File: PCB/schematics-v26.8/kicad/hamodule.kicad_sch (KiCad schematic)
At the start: 192 parts, among them J1 GND|5V, J10 Tx|Rx, J11 Sda|Scl, J12 3|9, J13 13|12, J14 3.3v|GND|7|15, J15 2604-1104, J16 2604-1104, J17 TestPoint, J19 TestPoint, J2 2604-1102, J3 USB_C_Receptacle_USB2.0, J4 GND|3.3V, J5 Conn_01x02_Pin, J6 2604-1104, J7 2604-1104, J8 5v|GND|Do, J9 Screen, K1 AQG22205, K2 AQG22205, K3 AQG22205, K4 AQG22205, K5 AQG22205, K6 AQG22205, K7 AQG22205, K8 AQG22205, SW1 USB | PS, SW2 Reset, SW3 Boot, U1 LD1117AV33, U10 SN74LV1T34DBV, U11 ULN2803A, U12 TCAL6416, U14 74AHC1G04, U2 USBLC6-2SC6, U3 ESP32-S3-WROOM-2, U4 LDA210, U5 LDA210, U6 LDA210, U7 LDA210, U8 SHT4x, U9 SN74LVCH8T245

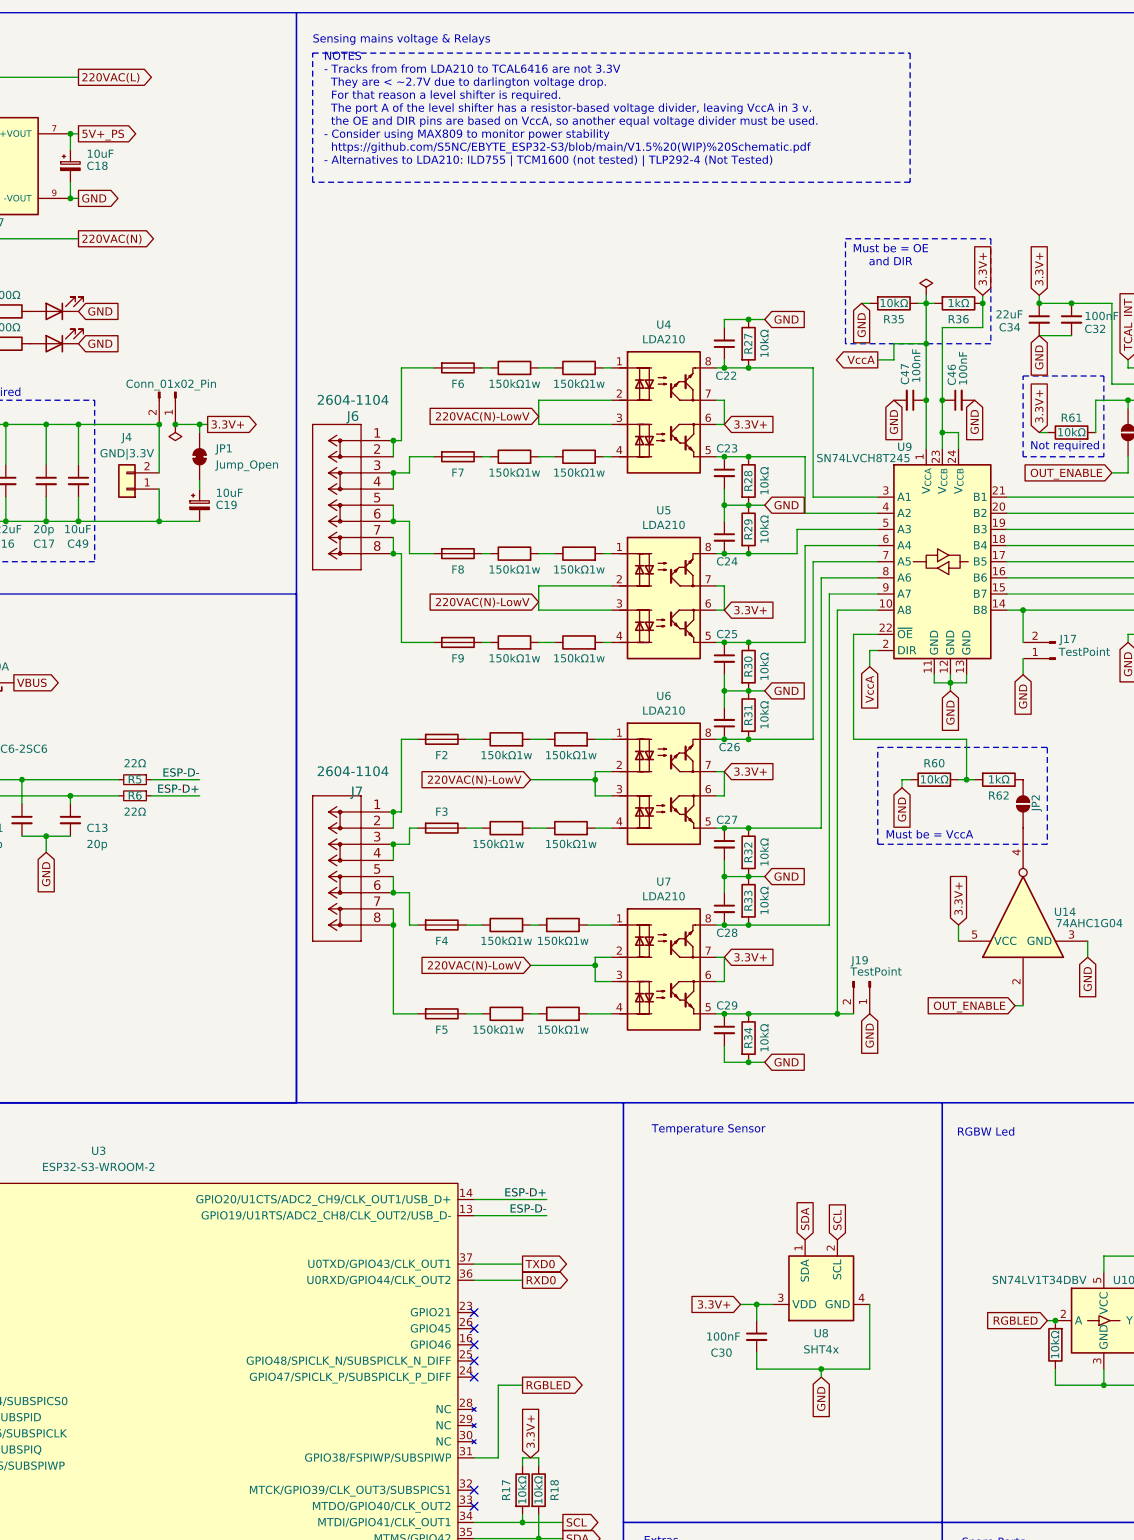
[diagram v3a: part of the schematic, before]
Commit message: [V26] Updated RST-80-AMMO (lib -> kicad_sym). Updated components to match library naming <library:footprint>. Utilize standard library for some components (SHT40, ULN). Updated LD1117 symbol to match the one used (THT vs SMD)
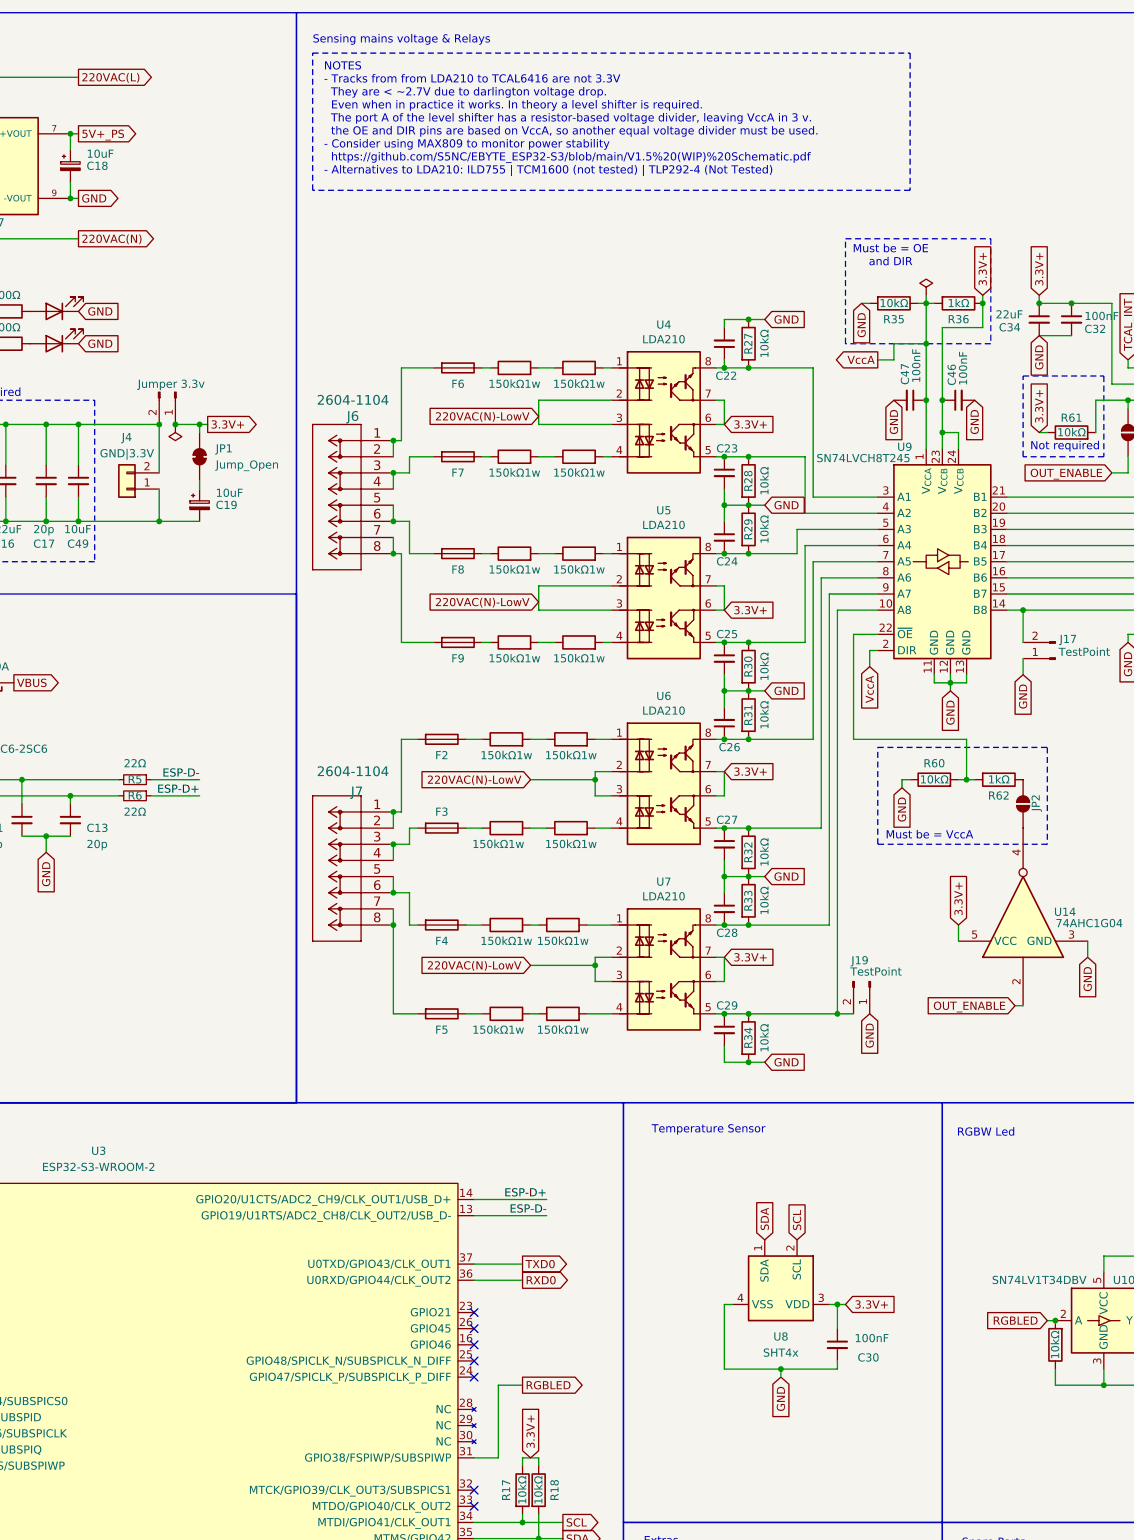
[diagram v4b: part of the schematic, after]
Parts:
- J5: value Conn_01x02_Pin -> Jumper 3.3v
- K1, K2, K3, K4, K5, K6, K7, K8: footprint AQG12205 -> AQG12205:AQG12205
- PS1: footprint CONV_RAC05-05SK/277 -> rac05-05sk:277
- U1: footprint Package_TO_SOT_SMD:SOT-223-3_TabPin2 -> Package_TO_SOT_THT:TO-220-3_Vertical; symbol Regulator_Linear:LD1117S33TR_SOT223 -> Regulator_Linear:LD1117V33
- U8: footprint Sensor:SHT4x -> Sensor_Humidity:Sensirion_DFN-4_1.5x1.5mm_P0.8mm_SHT4x_NoCentralPad; symbol sht40:SHT4x -> Sensor_Humidity:SHT4x
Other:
- note added: "NOTES - Tracks from from LDA210 to TCAL6416 are not 3.3V They are < ~2.7V due to darlington voltage drop. Even when in practice it works. In theory a level shifter is required. The port A of the level shifter has a resistor-based voltage divider, leaving VccA in 3 v. the OE and DIR pins are based on VccA, so another equal voltage divider must be used. - Consider using MAX809 to monitor power stab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"
- note removed: "NOTES - Tracks from from LDA210 to TCAL6416 are not 3.3V They are < ~2.7V due to darlington voltage drop. For that reason a level shifter is required. The port A of the level shifter has a resistor-based voltage divider, leaving VccA in 3 v. the OE and DIR pins are based on VccA, so another equal voltage divider must be used. - Consider using MAX809 to monitor power stability https://github.com/S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"
- moved on the sheet: C30, U8

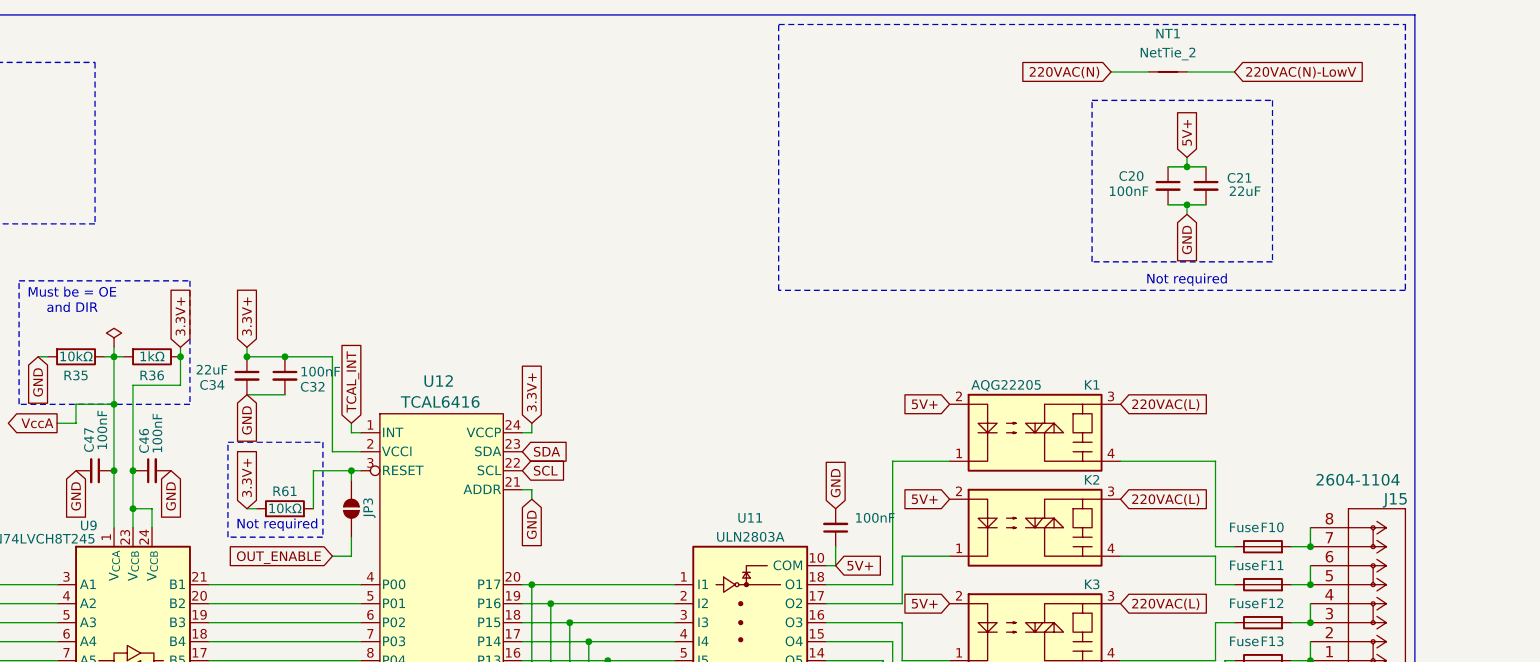
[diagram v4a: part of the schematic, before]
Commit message: Added 0201 capacitors for decoupling high frequencies. Reshuffled some resistors to make more straight paths. Added silkscreen where missing
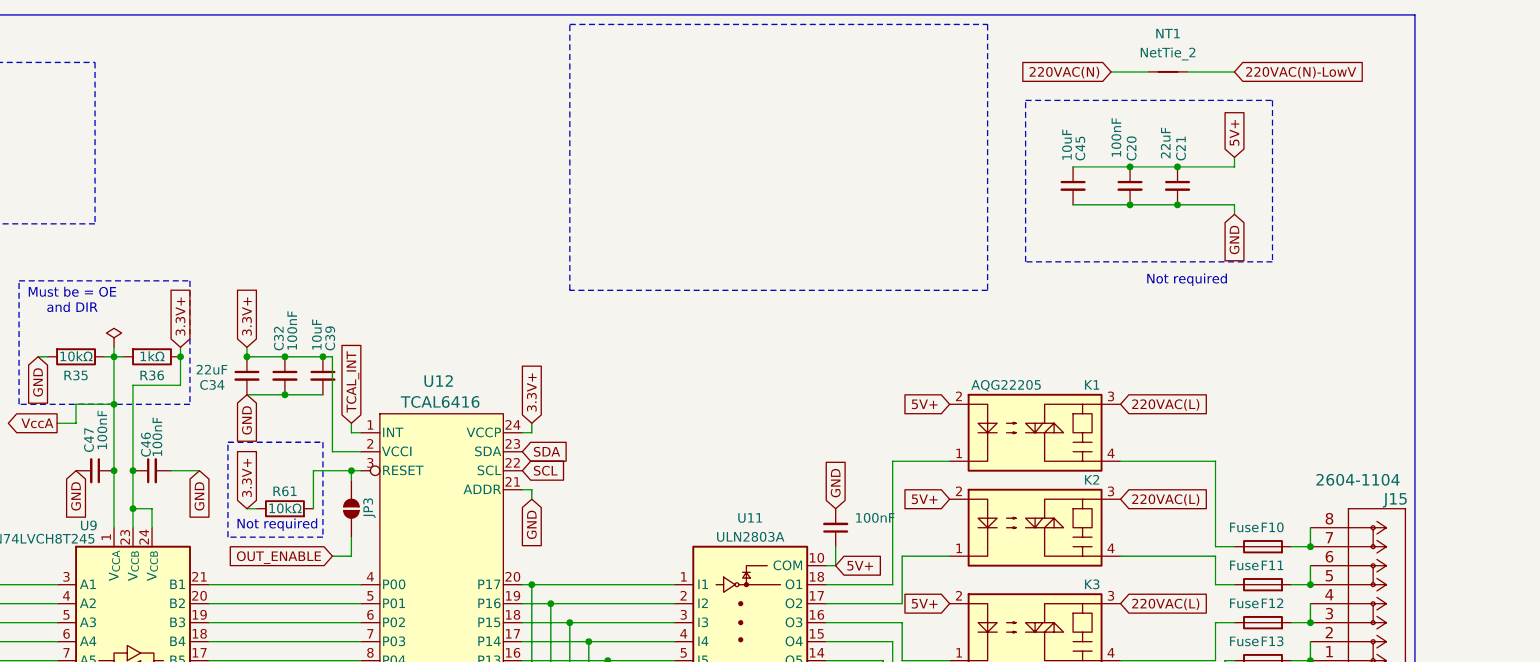
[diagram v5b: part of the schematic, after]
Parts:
- added C39, C45: 10uF, Capacitor_SMD:C_0402_1005Metric, symbol Device:C_Small
- C34: footprint Capacitor_SMD:C_0603_1608Metric_Pad1.08x0.95mm_HandSolder -> Capacitor_SMD:C_0805_2012Metric_Pad1.18x1.45mm_HandSolder
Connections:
- net 3.3V+: now also C39.1
- net 5V+: now also C45.1
- net GND: now also C39.2, C45.2
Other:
- moved on the sheet: C20, C21

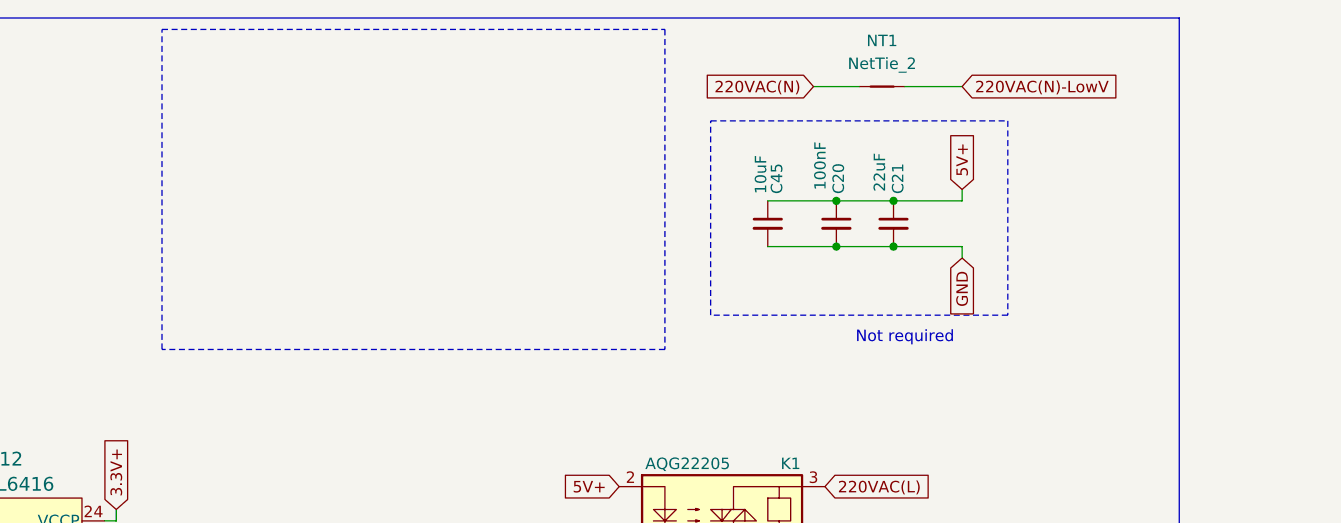
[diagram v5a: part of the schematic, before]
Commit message: Fixed library filters to allow selected footprint
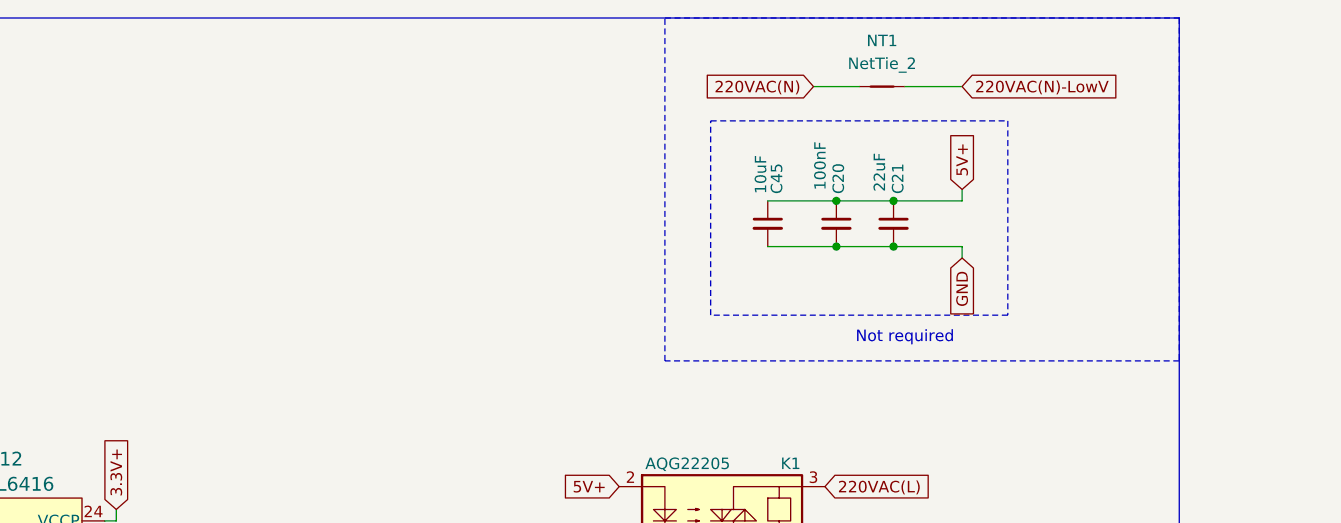
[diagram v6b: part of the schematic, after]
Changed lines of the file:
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@@
 	)
 	(rectangle
-		(start 294.64 13.97)
-		(end 350.52 49.53)
+		(start 350.52 12.7)
+		(end 407.67 50.8)
 		(stroke
 			(width 0)

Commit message: Created only one project specific symbol library, one for footprints, and one for icons. Deleted all the rest from the components folder
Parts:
- F10, F11, F12, F13, F14, F15, F16, F17, F2, F3, F4, F5, F6, F7, F8, F9: footprint RST-80-AMMO:FUSE_RST-1-BULK -> Hamodule_Footprints:FUSE_RST-1-BULK
- J15, J16, J6, J7: footprint wago-2604-1104:big_pads_2604-1104 -> Hamodule_Footprints:WAGO_2604-1104; symbol wago-2604-1104:2604-1104 -> Hamodule_Symbols:2604-1104
- J2: footprint wago-2604-1102:big_pads_2604-1102 -> Hamodule_Footprints:WAGO-2604-1102; symbol wago-2604-1102:2604-1102 -> Hamodule_Symbols:2604-1102
- J3: footprint usb-c:USB_C_Receptacle_HRO_TYPE-C-31-M-12 -> Connector_USB:USB_C_Receptacle_HRO_TYPE-C-31-M-12
- K1, K2, K3, K4, K5, K6, K7, K8: footprint AQG12205:AQG12205 -> Hamodule_Footprints:AQG12205; symbol AQG12205:AQG12205 -> Hamodule_Symbols:AQG12205
- PS1: footprint rac05-05sk:277 -> Hamodule_Footprints:RAC05-05SK_277; symbol RAC05-05SK_277:RAC05-05SK/277 -> Hamodule_Symbols:RAC05-05SK/277
- SW2, SW3: footprint hamodule_SW_SPST_SKQG_WithStem:SW_SPST_SKQG_WithStem -> Button_Switch_SMD:SW_SPST_SKQG_WithStem
- U12: symbol hamodule_library:TCAL6416 -> Hamodule_Symbols:TCAL6416
- U3: footprint Espressif:ESP32-S3-WROOM-2 -> Hamodule_Footprints:ESP32-S3-WROOM-2; symbol Espressif:ESP32-S3-WROOM-2 -> Hamodule_Symbols:ESP32-S3-WROOM-2
- U4, U5, U6, U7: symbol LDA210-PDIP:LDA210-PDIP -> Hamodule_Symbols:LDA210
- U9: symbol sn74lvch8t245:SN74LVCH8T245 -> Hamodule_Symbols:SN74LVCH8T245
